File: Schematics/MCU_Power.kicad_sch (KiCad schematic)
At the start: 1 part

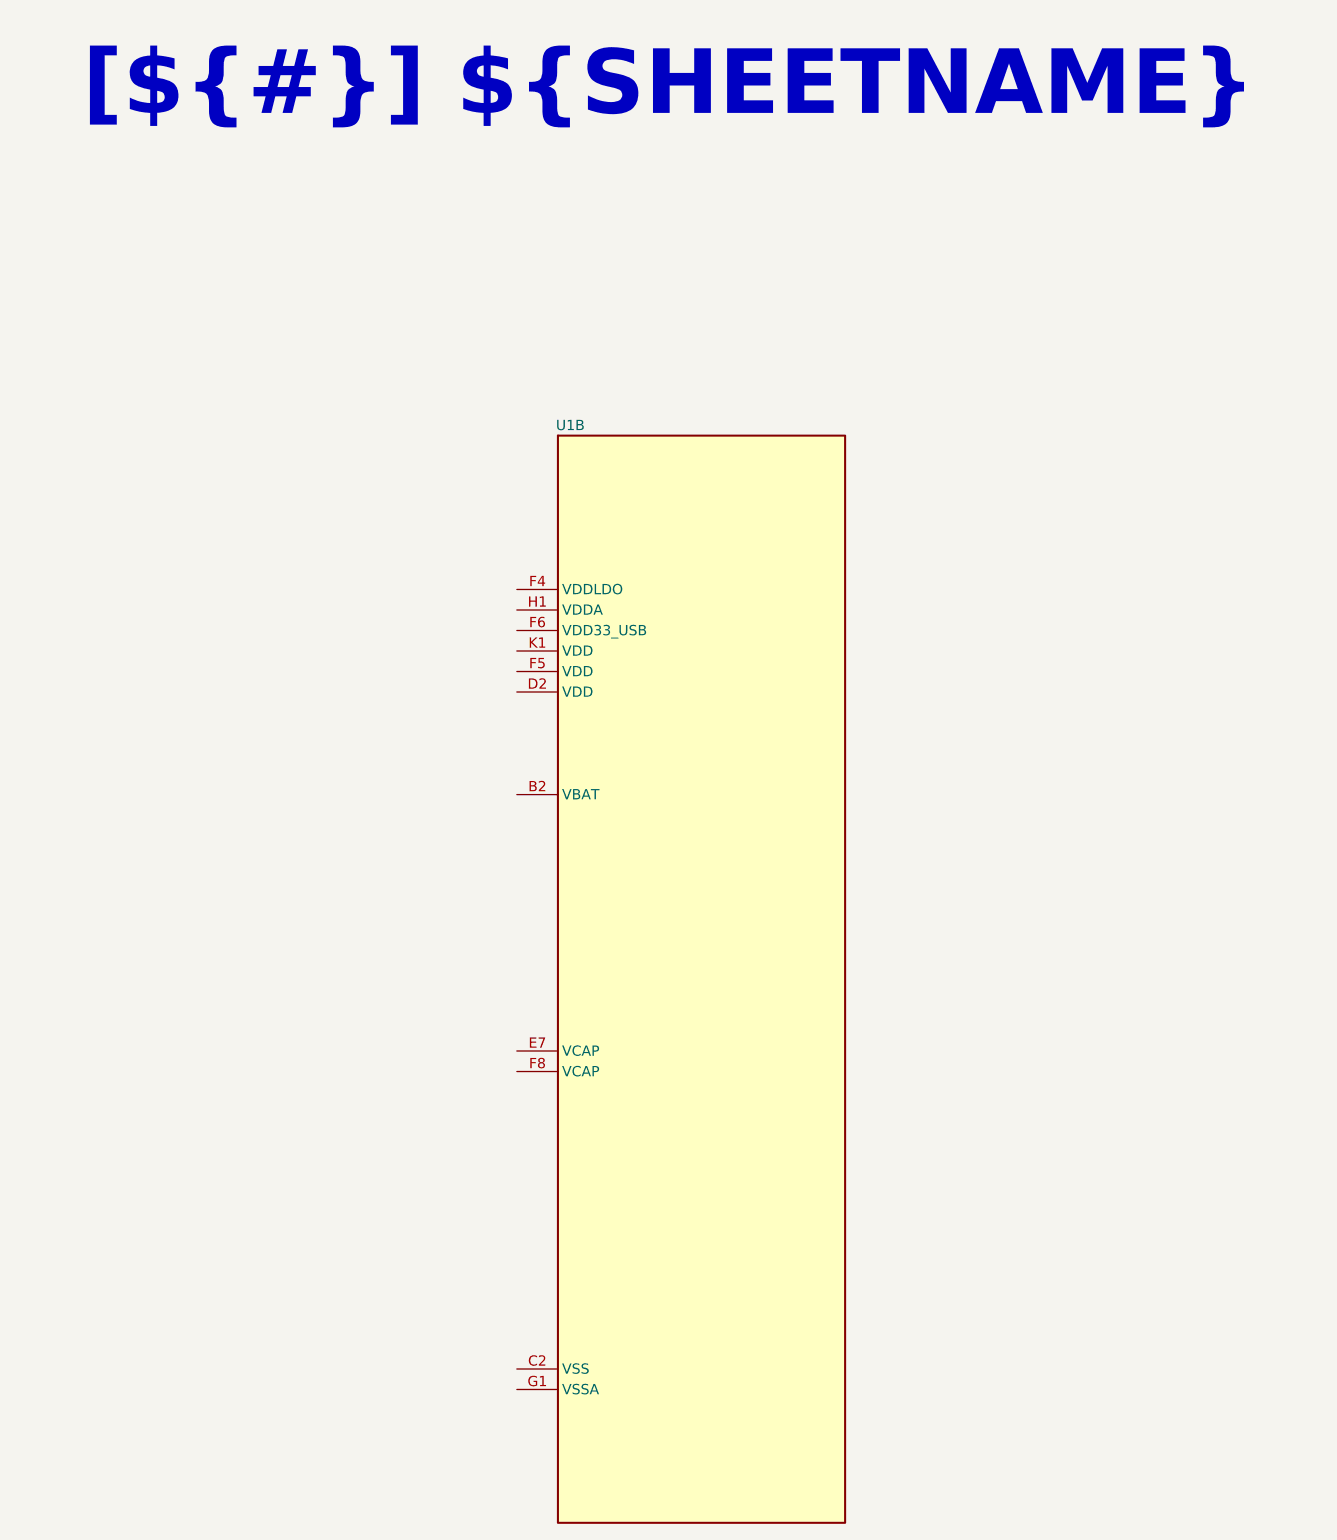
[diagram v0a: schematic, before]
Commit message: Add MCU Power schematic
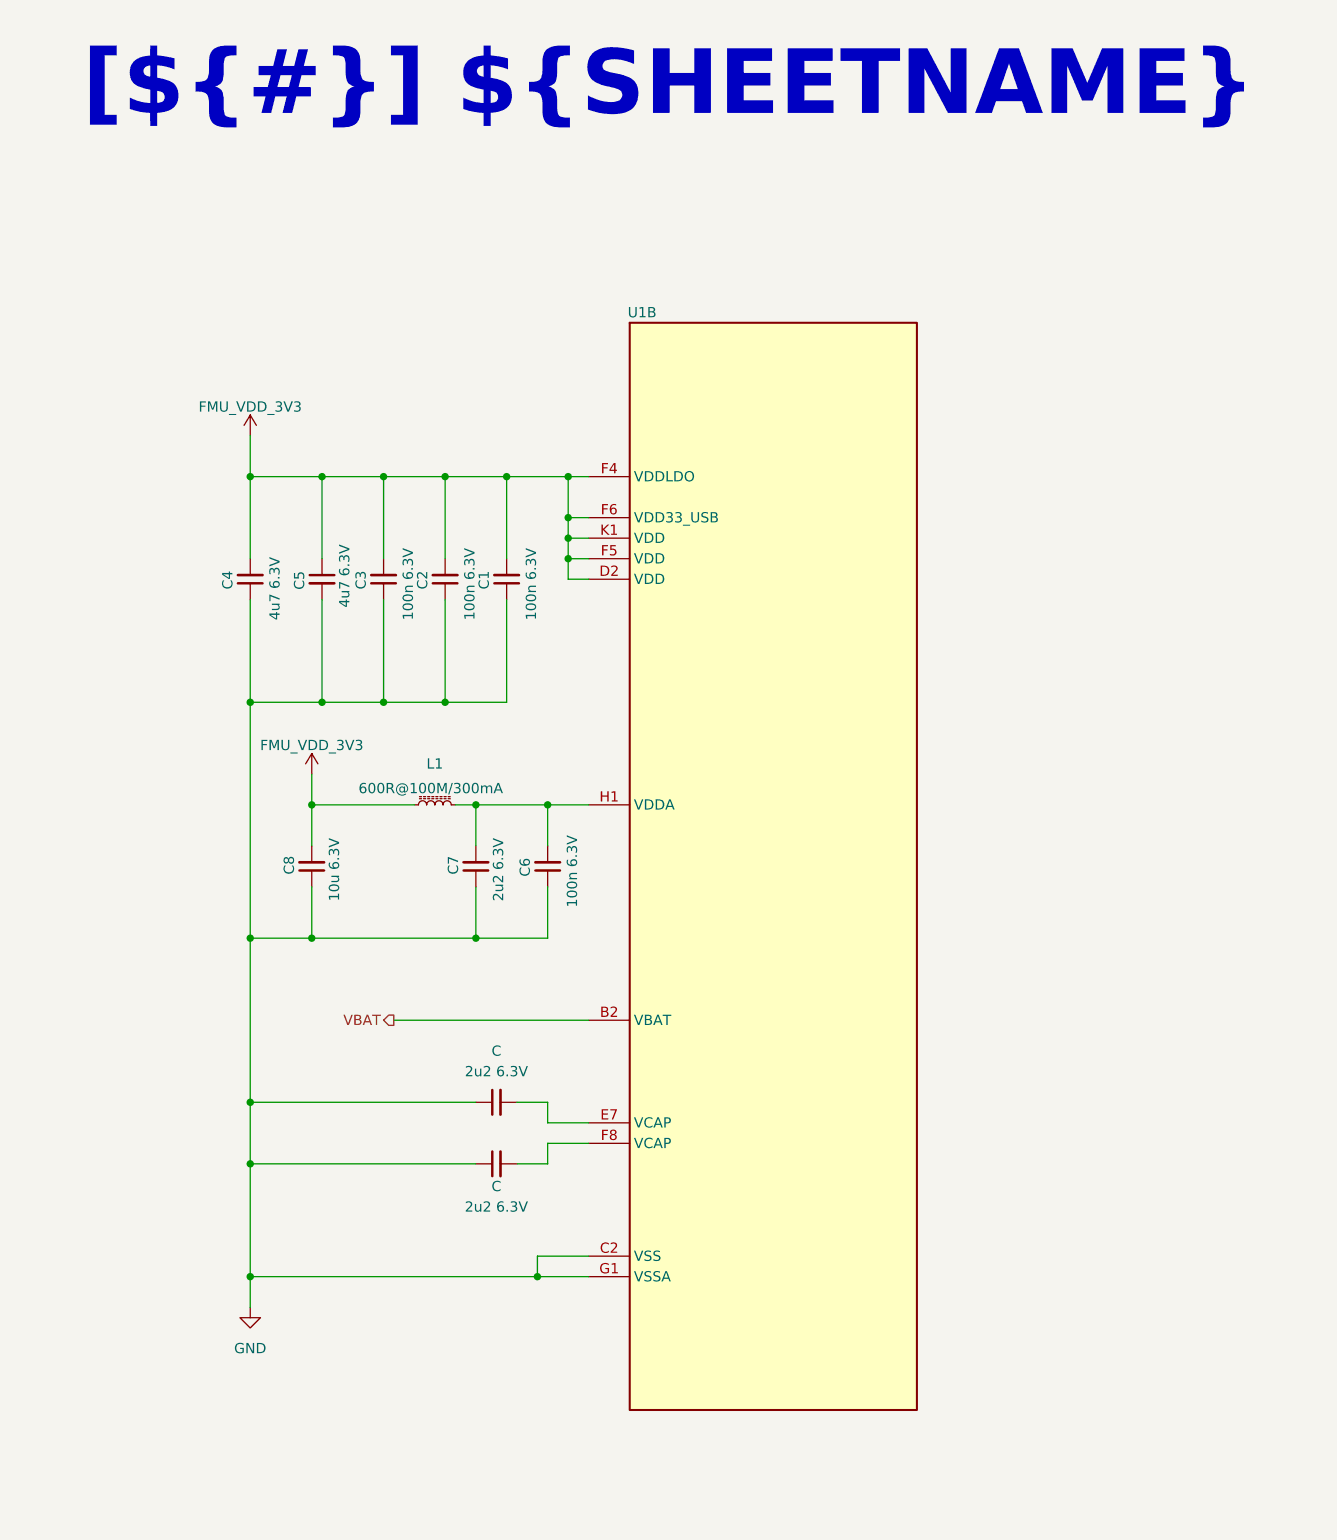
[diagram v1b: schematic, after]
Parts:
- added C (x2), C7: 2u2 6.3V, Capacitor_SMD:C_0603_1608Metric, symbol Device:C_Small
- added C1, C2, C3, C6: 100n 6.3V, Capacitor_SMD:C_0603_1608Metric, symbol Device:C_Small
- added C4, C5: 4u7 6.3V, Capacitor_SMD:C_0603_1608Metric, symbol Device:C_Small
- added C8: 10u 6.3V, Capacitor_SMD:C_0603_1608Metric, symbol Device:C_Small
- added L1: 600R@100M/300mA, symbol Device:L_Ferrite_Small
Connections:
- net VBAT: now reaches U1.B2 (VBAT)
- net GND: now reaches U1.C2 (VSS), U1.E4 (VSS), U1.E5 (VSS), U1.E6 (VSS), U1.J1 (VSS)
- net GND: now also U1.G1 (VSSA), C.1, C.1, C1.1, C2.1, C3.1, C4.1, C5.2, C6.1, C7.1, C8.1
- net FMU_VDD_3V3: now reaches U1.D2 (VDD)
- net FMU_VDD_3V3: now also U1.F4 (VDDLDO), U1.F5 (VDD), U1.F6 (VDD33_USB), U1.K1 (VDD), C1.2, C2.2, C3.2, C4.2, C5.1, C8.2, L1.1
- net at U1.E7 (VCAP): now also C.2
- net at U1.F8 (VCAP): now also C.2
- net at U1.H1 (VDDA): now also C6.2, C7.2, L1.2
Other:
- moved on the sheet: U1B
